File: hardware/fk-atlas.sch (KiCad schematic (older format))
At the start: 62 parts, among them J1 CONN_02x05_SWD, J2 MICRO-USB, J3 CONN_01x02, J4 CONN_01x03_SERIAL, J5 CONN_01x05, J6 CONN_01x04, J7 CONN_01x05, J8 CONN_01x02, M1 MOUNT_HOLE, M2 MOUNT_HOLE, M3 MOUNT_HOLE, M4 MOUNT_HOLE, M5 FIDUCIAL, M6 FIDUCIAL, M7 FIDUCIAL, Q4 2N7002LT1G, SW1 SPNO, U1 S25FL116K0XMFI041, U2 ATSAMD21G18A-AU, U3 MCP1700T-3302E/MB, U4 TPS2052B, U5 SK6812, Y1 FC-135

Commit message: Adding some pull downs.
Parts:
- added R13, R14: ?, conservify:RES-0603, symbol conservify:RESISTOR
- R3, R6: value 10K -> ?; MFP RC0603FR-0710KL -> ?; spn1 603-RC0603FR-0710KL -> ?
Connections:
- wire segments 282 -> 287
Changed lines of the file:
@@
 P 7300 9950
 F 0 "R3" H 7450 10050 60  0000 C CNN
-F 1 "10K" H 7300 10050 60  0000 C CNN
+F 1 "?" H 7300 10050 60  0000 C CNN
 F 2 "conservify:RES-0603" H 7300 9750 60  0001 C CNN
 F 3 "" H 7300 9950 60  0000 C CNN
 F 4 " " H 7250 9850 50  0001 C CNN "Critical"
 F 5 "Yageo" H 7250 9850 50  0001 C CNN "MFN"
-F 6 "RC0603FR-0710KL" H 7250 9850 50  0001 C CNN "MFP"
+F 6 "?" H 7250 9850 50  0001 C CNN "MFP"
 F 7 " " H 7250 9850 50  0001 C CNN "Notes"
 F 8 " " H 7250 9850 50  0001 C CNN "Package"
@@
 F 10 " " H 7250 9850 50  0001 C CNN "Subsystem"
 F 11 "0" H 7250 9850 50  0001 C CNN "price"
-F 12 "603-RC0603FR-0710KL" H 3250 8650 50  0001 C CNN "spn1"
+F 12 "?" H 3250 8650 50  0001 C CNN "spn1"
 F 13 "mouser" H 3250 8650 50  0001 C CNN "supplier1"
 	1    7300 9950
@@
 P 7500 10050
 F 0 "R6" H 7650 10150 60  0000 C CNN
-F 1 "10K" H 7500 10150 60  0000 C CNN
+F 1 "?" H 7500 10150 60  0000 C CNN
 F 2 "conservify:RES-0603" H 7500 9850 60  0001 C CNN
 F 3 "" H 7500 10050 60  0000 C CNN
 F 4 " " H 7450 9950 50  0001 C CNN "Critical"
 F 5 "Yageo" H 7450 9950 50  0001 C CNN "MFN"
-F 6 "RC0603FR-0710KL" H 7450 9950 50  0001 C CNN "MFP"
+F 6 "?" H 7450 9950 50  0001 C CNN "MFP"
 F 7 " " H 7450 9950 50  0001 C CNN "Notes"
 F 8 " " H 7450 9950 50  0001 C CNN "Package"
@@
 F 10 " " H 7450 9950 50  0001 C CNN "Subsystem"
 F 11 "0" H 7450 9950 50  0001 C CNN "price"
-F 12 "603-RC0603FR-0710KL" H 3450 8750 50  0001 C CNN "spn1"
+F 12 "?" H 3450 8750 50  0001 C CNN "spn1"
 F 13 "mouser" H 3450 8750 50  0001 C CNN "supplier1"
 	1    7500 10050
@@
 Wire Wire Line
 	7300 10400 7300 10200
+Text Label 8350 10750 0    50   ~ 0
+PERIPH_3V3
+Text Label 8350 10900 0    50   ~ 0
+ATLAS_3V3
+$Comp
+L conservify:GND #PWR0110
+U 1 1 5C83031F
+P 9850 10900
+F 0 "#PWR0110" H 9850 10650 50  0001 C CNN
+F 1 "GND" H 9850 10750 50  0000 C CNN
+F 2 "" H 9850 10900 50  0001 C CNN
+F 3 "" H 9850 10900 50  0001 C CNN
+	1    9850 10900
+	1    0    0    -1
+$EndComp
+$Comp
+L conservify:RESISTOR R13
+U 1 1 5C846C44
+P 9100 10750
+F 0 "R13" H 8900 10700 60  0000 C CNN
+F 1 "?" H 9300 10700 60  0000 C CNN
+F 2 "conservify:RES-0603" H 9100 10550 60  0001 C CNN
+F 3 "" H 9100 10750 60  0000 C CNN
+F 4 " " H 9050 10650 50  0001 C CNN "Critical"
+F 5 "Yageo" H 9050 10650 50  0001 C CNN "MFN"
+F 6 "?" H 9050 10650 50  0001 C CNN "MFP"
+F 7 " " H 9050 10650 50  0001 C CNN "Notes"
+F 8 " " H 9050 10650 50  0001 C CNN "Package"
+F 9 "ANY" H 9050 10650 50  0001 C CNN "Source"
+F 10 " " H 9050 10650 50  0001 C CNN "Subsystem"
+F 11 "0" H 9050 10650 50  0001 C CNN "price"
+F 12 "?" H 5050 9450 50  0001 C CNN "spn1"
+F 13 "mouser" H 5050 9450 50  0001 C CNN "supplier1"
+	1    9100 10750
+	1    0    0    -1
+$EndComp
+$Comp
+L conservify:RESISTOR R14
+U 1 1 5C85D2AF
+P 9100 10900
+F 0 "R14" H 8900 10850 60  0000 C CNN
+F 1 "?" H 9300 10850 60  0000 C CNN
+F 2 "conservify:RES-0603" H 9100 10700 60  0001 C CNN
+F 3 "" H 9100 10900 60  0000 C CNN
+F 4 " " H 9050 10800 50  0001 C CNN "Critical"
+F 5 "Yageo" H 9050 10800 50  0001 C CNN "MFN"
+F 6 "?" H 9050 10800 50  0001 C CNN "MFP"
+F 7 " " H 9050 10800 50  0001 C CNN "Notes"
+F 8 " " H 9050 10800 50  0001 C CNN "Package"
+F 9 "ANY" H 9050 10800 50  0001 C CNN "Source"
+F 10 " " H 9050 10800 50  0001 C CNN "Subsystem"
+F 11 "0" H 9050 10800 50  0001 C CNN "price"
+F 12 "?" H 5050 9600 50  0001 C CNN "spn1"
+F 13 "mouser" H 5050 9600 50  0001 C CNN "supplier1"
+	1    9100 10900
+	1    0    0    -1
+$EndComp
+Wire Wire Line
+	8350 10750 8850 10750
+Wire Wire Line
+	8850 10900 8350 10900
+Wire Wire Line
+	9350 10750 9850 10750
+Wire Wire Line
+	9850 10750 9850 10900
+Wire Wire Line
+	9350 10900 9850 10900
+Connection ~ 9850 10900
 $EndSCHEMATC

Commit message: Mounting holes are 2.7mm. Plotting.
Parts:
- M1, M2, M3, M4: footprint conservify:HOLE_NPTH_2.54MM -> conservify:HOLE_NPTH_2.7MM
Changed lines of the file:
@@
 F 0 "M1" H 1150 10700 50  0000 C CNN
 F 1 "MOUNT_HOLE" H 1150 10400 50  0001 C CNN
-F 2 "conservify:HOLE_NPTH_2.54MM" H 1175 10325 50  0001 C CNN
+F 2 "conservify:HOLE_NPTH_2.7MM" H 1175 10325 50  0001 C CNN
 F 3 "" H 1150 10550 50  0000 C CNN
 F 4 " " H 1150 10800 50  0001 C CNN "Critical"
@@
 F 0 "M2" H 1450 10700 50  0000 C CNN
 F 1 "MOUNT_HOLE" H 1450 10400 50  0001 C CNN
-F 2 "conservify:HOLE_NPTH_2.54MM" H 1475 10325 50  0001 C CNN
+F 2 "conservify:HOLE_NPTH_2.7MM" H 1475 10325 50  0001 C CNN
 F 3 "" H 1450 10550 50  0000 C CNN
 F 4 " " H 1450 10800 50  0001 C CNN "Critical"
@@
 F 0 "M3" H 1750 10700 50  0000 C CNN
 F 1 "MOUNT_HOLE" H 1750 10400 50  0001 C CNN
-F 2 "conservify:HOLE_NPTH_2.54MM" H 1775 10325 50  0001 C CNN
+F 2 "conservify:HOLE_NPTH_2.7MM" H 1775 10325 50  0001 C CNN
 F 3 "" H 1750 10550 50  0000 C CNN
 F 4 " " H 1750 10800 50  0001 C CNN "Critical"
@@
 F 0 "M4" H 2050 10700 50  0000 C CNN
 F 1 "MOUNT_HOLE" H 2050 10400 50  0001 C CNN
-F 2 "conservify:HOLE_NPTH_2.54MM" H 2075 10325 50  0001 C CNN
+F 2 "conservify:HOLE_NPTH_2.7MM" H 2075 10325 50  0001 C CNN
 F 3 "" H 2050 10550 50  0000 C CNN
 F 4 " " H 2050 10800 50  0001 C CNN "Critical"

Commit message: Add orientation indicator to SWD fp.
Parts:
- R13, R14, R3, R6: MFN Yageo -> (none); MFP ? -> (none); spn1 ? -> (none)
- U4: Critical (none) -> (none); MFN (none) -> Texas Instruments; MFP (none) -> TPS2052BDR; Notes (none) -> (none); Package (none) -> (none); SPN1 (none) -> 296-17451-1-ND; Source (none) -> ANY; Subsystem (none) -> (none); Supplier1 (none) -> digikey

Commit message: Started transition to 4 layer board
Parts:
- added J?: MICRO-USB, conservify:MICRO-USB, symbol fk-atlas-rescue:MICRO_USB-conservify
- C1, C10, C11, C12, C13, C14, C15, C16, C17, C18, C19, C2, C20, C21, C3, C4, C5, C6, C7, C8, C9: symbol conservify:CAPACITOR_CERAMIC -> fk-atlas-rescue:CAPACITOR_CERAMIC-conservify
- D4: symbol conservify:LED_SINGLE -> fk-atlas-rescue:LED_SINGLE-conservify
- D5: symbol conservify:PRTR5V0U2X -> fk-atlas-rescue:PRTR5V0U2X-conservify
- D6: symbol conservify:DIODE_DUAL_SCHOTTKY -> fk-atlas-rescue:DIODE_DUAL_SCHOTTKY-conservify
- F1: symbol conservify:FUSE -> fk-atlas-rescue:FUSE-conservify
- J1: symbol conservify:CONN_02x05_SWD -> fk-atlas-rescue:CONN_02x05_SWD-conservify
- J2: symbol conservify:MICRO_USB -> fk-atlas-rescue:MICRO_USB-conservify
- J3, J8: symbol conservify:CONN_01x02 -> fk-atlas-rescue:CONN_01x02-conservify
- J4: symbol conservify:CONN_01x03_SERIAL -> fk-atlas-rescue:CONN_01x03_SERIAL-conservify
- J5, J7: symbol conservify:CONN_01x05 -> fk-atlas-rescue:CONN_01x05-conservify
- J6: symbol conservify:CONN_01x04 -> fk-atlas-rescue:CONN_01x04-conservify
- L1, L2: symbol conservify:INDUCTOR -> fk-atlas-rescue:INDUCTOR-conservify
- M1, M2, M3, M4: footprint conservify:HOLE_NPTH_2.7MM -> conservify:HOLE_NPTH_2.54MM; symbol conservify:MOUNT_HOLE -> fk-atlas-rescue:MOUNT_HOLE-conservify
- M5, M6, M7: symbol conservify:FIDUCIAL -> fk-atlas-rescue:FIDUCIAL-conservify
- Q4: symbol conservify:MOSFET_N -> fk-atlas-rescue:MOSFET_N-conservify
- R1, R10, R11, R12, R2, R4, R5, R7, R8, R9: symbol conservify:RESISTOR -> fk-atlas-rescue:RESISTOR-conservify
- R13, R14, R3, R6: symbol conservify:RESISTOR -> fk-atlas-rescue:RESISTOR-conservify; MFN (none) -> Yageo; MFP (none) -> ?; spn1 (none) -> ?
- SW1: symbol conservify:SWITCH_CONN_02 -> fk-atlas-rescue:SWITCH_CONN_02-conservify
- U1: symbol conservify:S25FL1xxK0XM -> fk-atlas-rescue:S25FL1xxK0XM-conservify
- U2: symbol conservify:ATSAMD21G18A_AU -> fk-atlas-rescue:ATSAMD21G18A_AU-conservify
- U3: symbol conservify:MCP1700T-XXX2E -> fk-atlas-rescue:MCP1700T-XXX2E-conservify
- U4: symbol conservify:TPS2052B -> fk-atlas-rescue:TPS2052B-conservify; Critical (none) -> (none); MFN Texas Instruments -> (none); MFP TPS2052BDR -> (none); Notes (none) -> (none); Package (none) -> (none); SPN1 296-17451-1-ND -> (none); Source ANY -> (none); Subsystem (none) -> (none); Supplier1 digikey -> (none)
- U5: symbol conservify:SK6812 -> fk-atlas-rescue:SK6812-conservify
- Y1: symbol conservify:CRYSTAL -> fk-atlas-rescue:CRYSTAL-conservify
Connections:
- wire segments 287 -> 299
- no-connect marks 25 -> 28

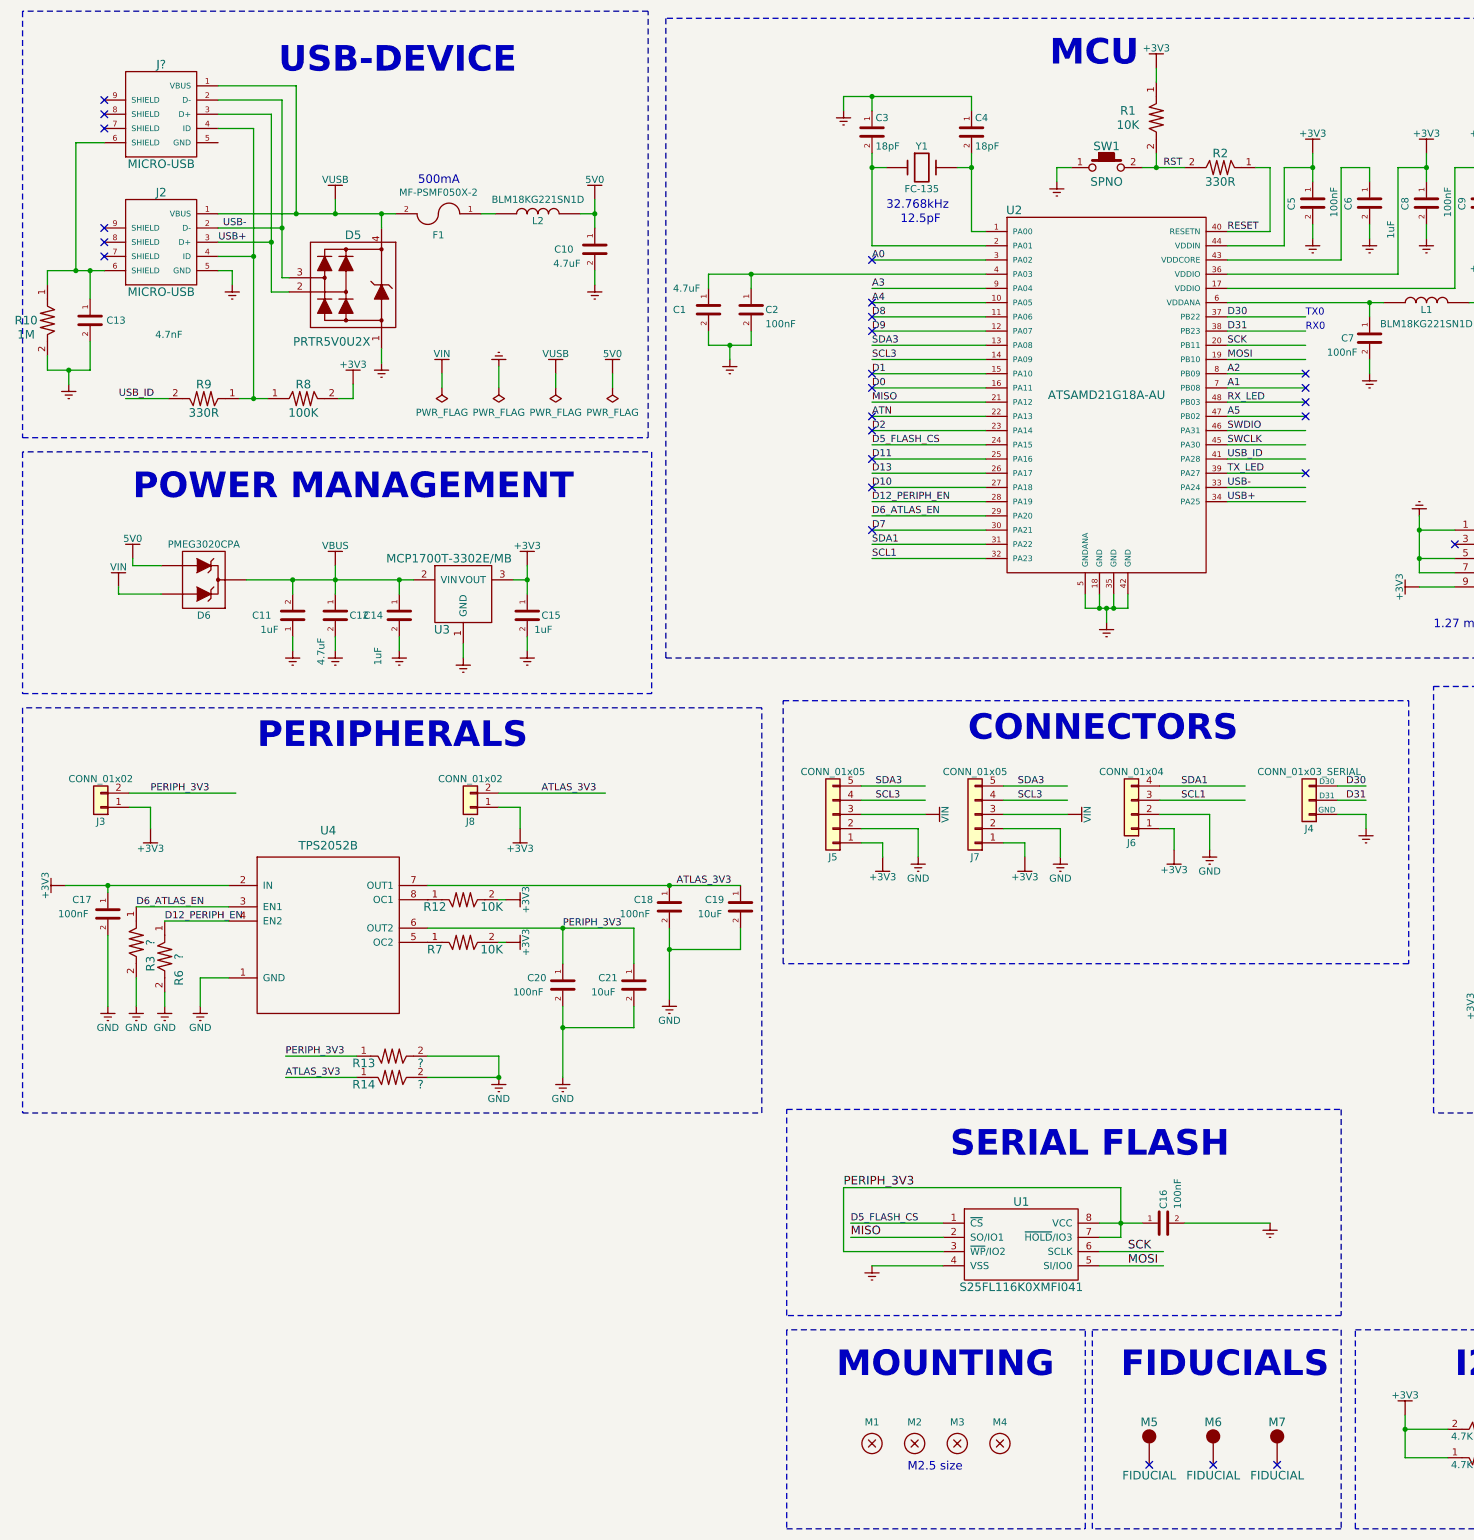
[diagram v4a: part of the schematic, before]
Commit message: Swapped out the USB connectors and added a second connector for the 'sensor' using the qwiic connector
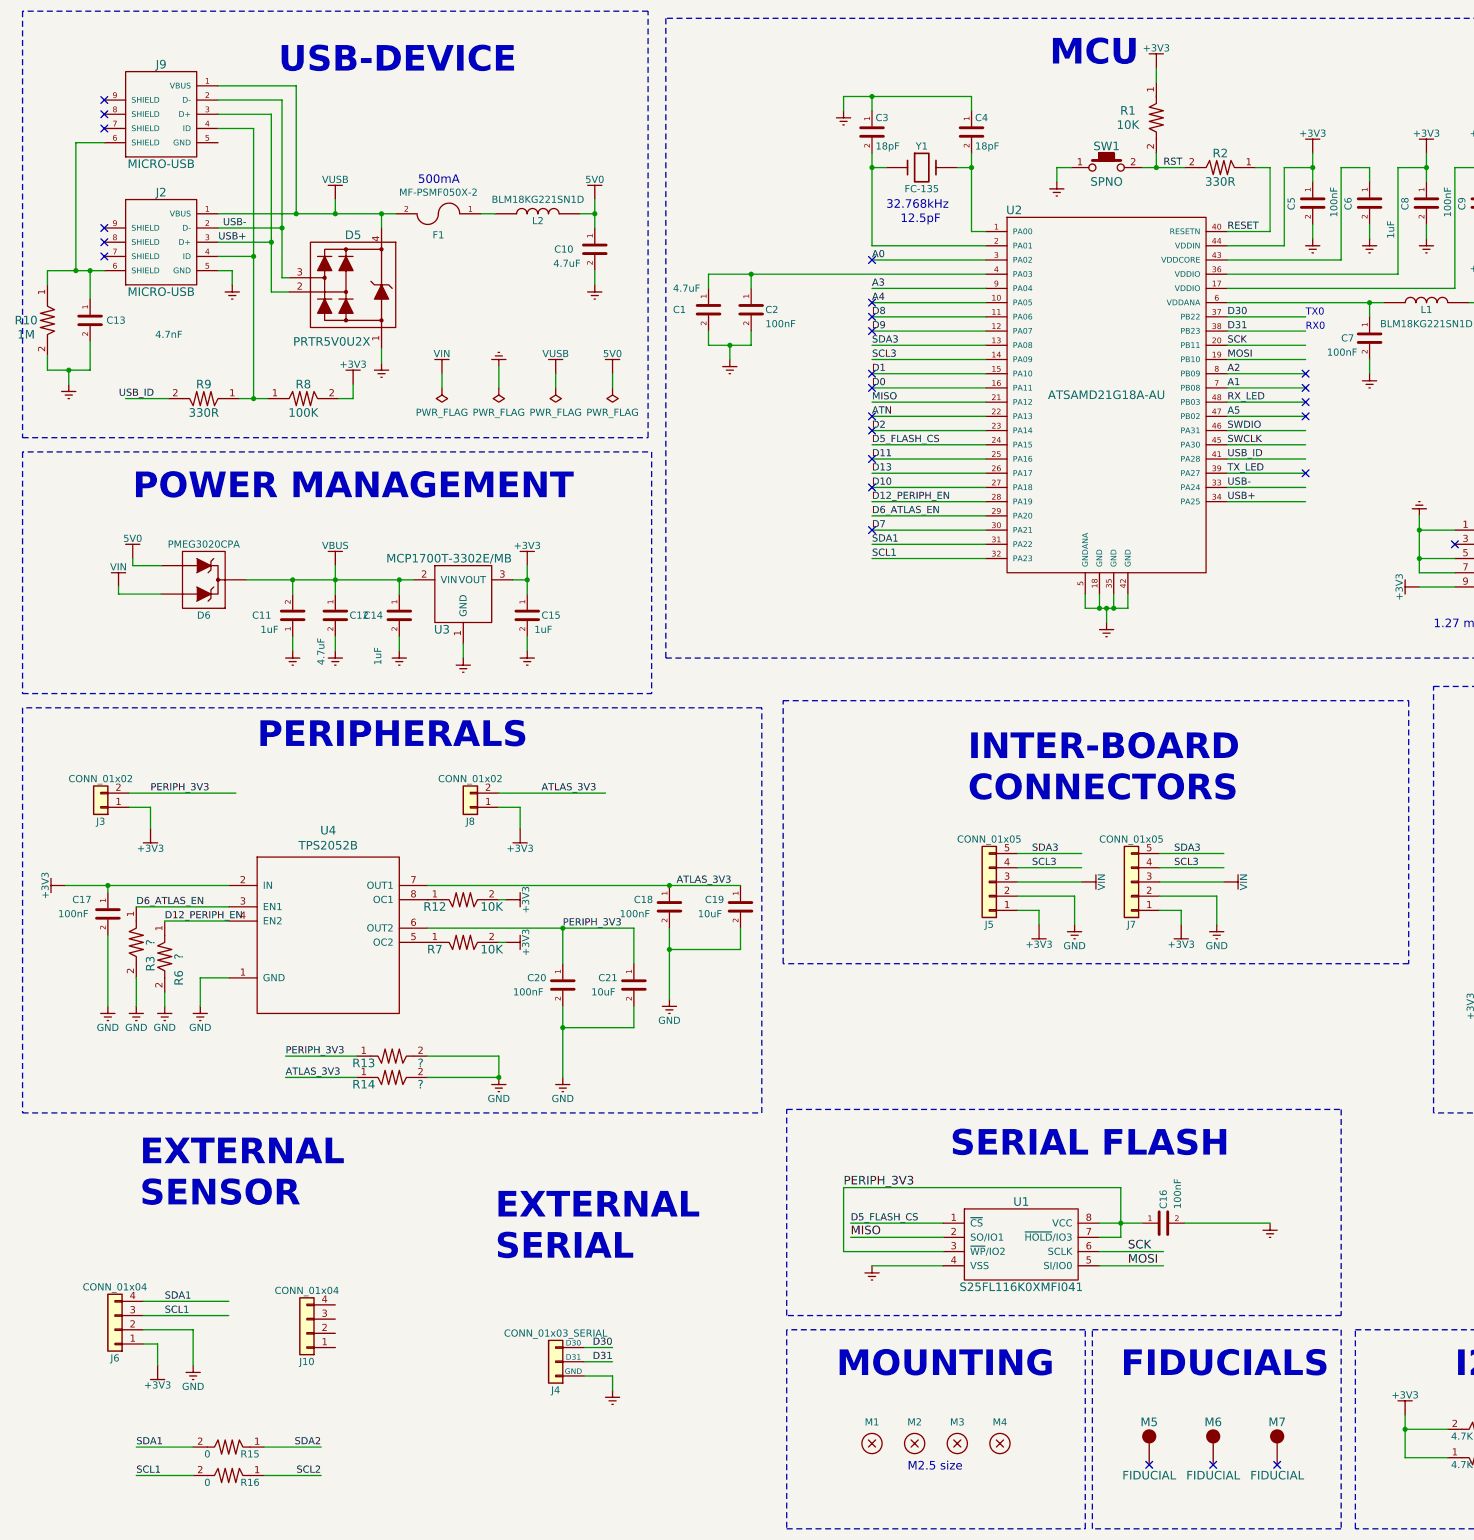
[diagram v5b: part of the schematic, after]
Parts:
- added J10: CONN_01x04, conservify:Molex_CLIK-Mate_502382-0470_1x04_P1.25mm_Vertical, symbol fk-atlas-rescue:CONN_01x04-conservify
- added R15, R16: 0, conservify:RES-0603, symbol fk-atlas-rescue:RESISTOR-conservify
- J2: footprint conservify:MICRO-USB -> conservify:USB_1051330011
- J9: renamed from J?; footprint conservify:MICRO-USB -> conservify:USB_10118193-0001LF-core-mod
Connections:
- net labels added: SCL2, SDA2
- wire segments 299 -> 303
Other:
- note added: "EXTERNAL \nSENSOR"
- note added: "EXTERNAL \nSERIAL"
- note added: "INTER-BOARD\nCONNECTORS"
- note removed: "CONNECTORS"
- moved on the sheet: J4, J5, J6, J7
